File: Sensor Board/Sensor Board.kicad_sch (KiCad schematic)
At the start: 30 parts, among them J1 Programming Header, J4 Micro_SD_Card, U1 PIC18F26K83, U3 SPX3819M5-L-3-3, U4 MCP2562, Y1 12MHz Crystal

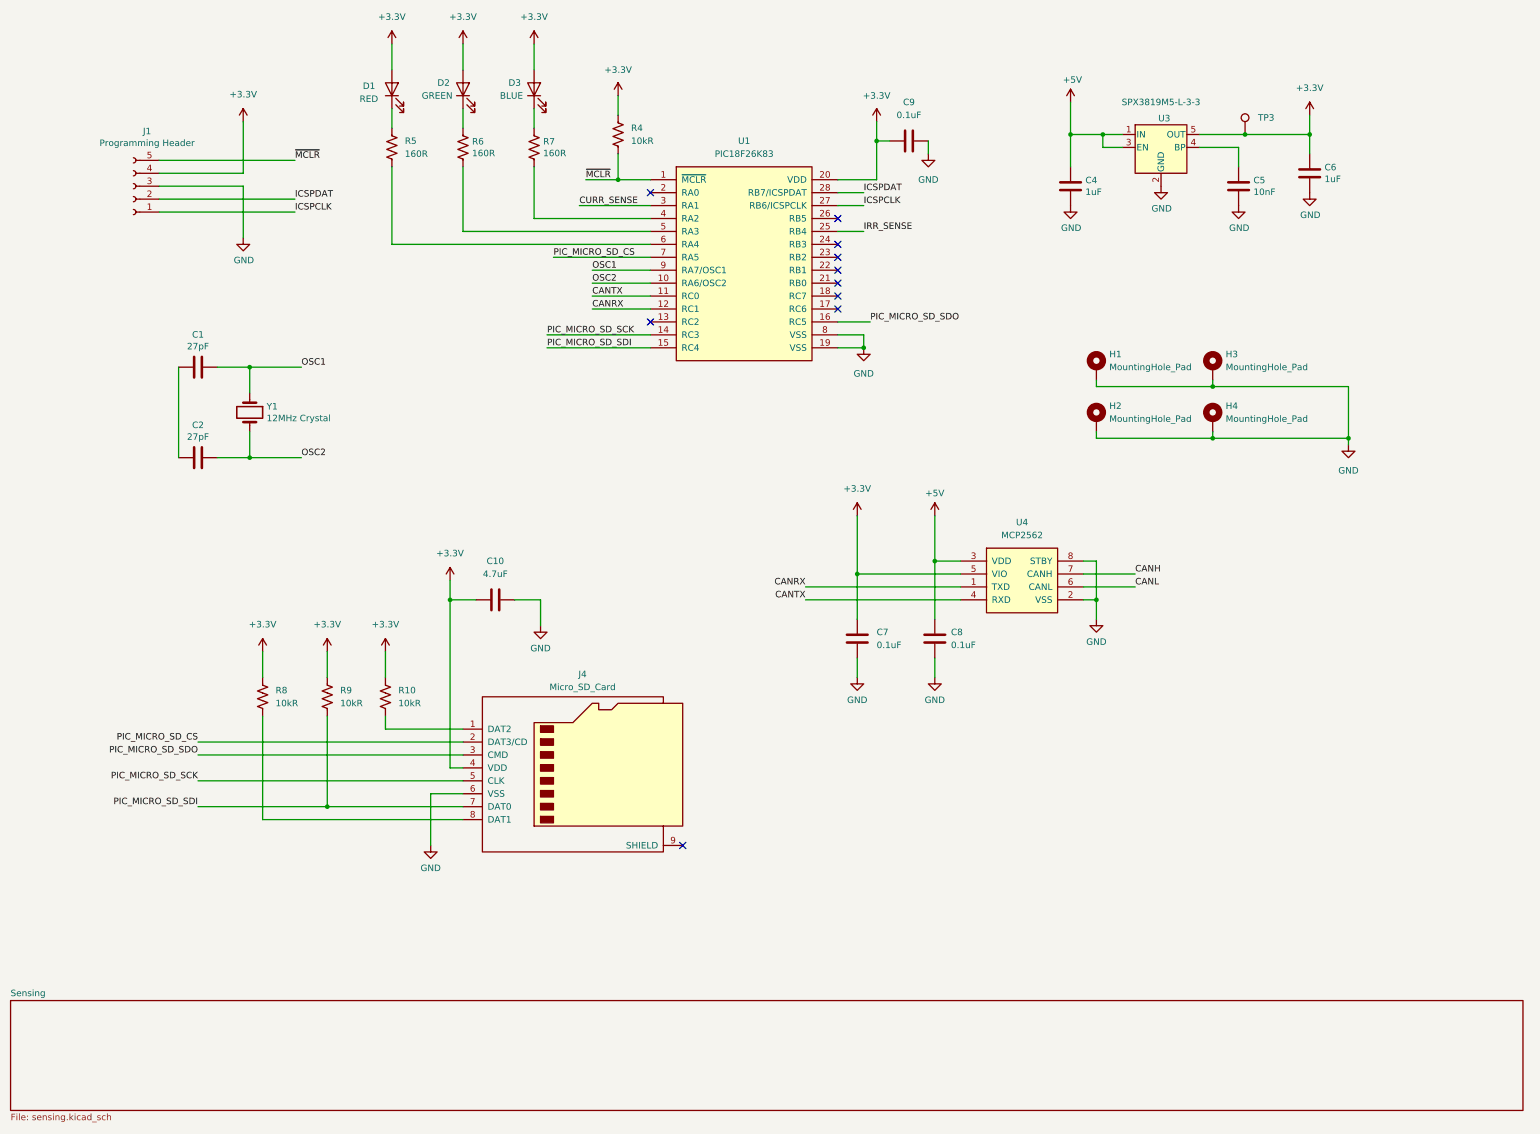
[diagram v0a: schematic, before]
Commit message: Finish schematics and footprint assignments
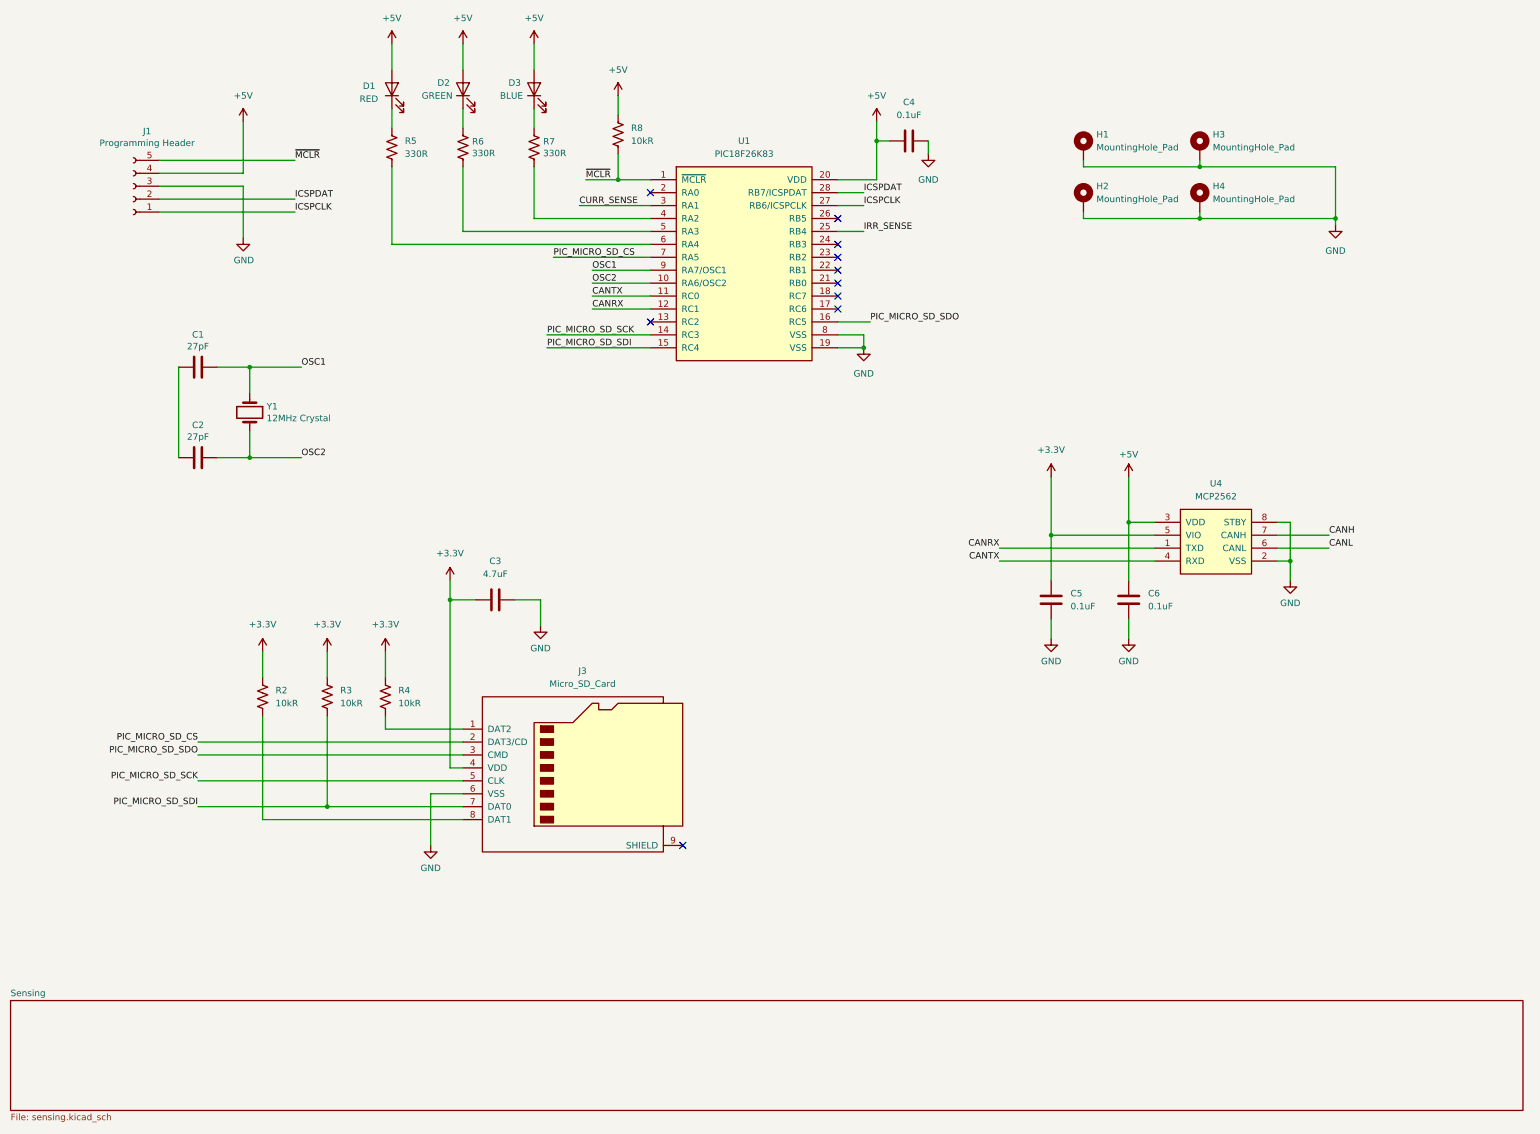
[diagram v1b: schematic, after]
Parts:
- removed C4, C6: 1uF, Capacitor_SMD:C_0805_2012Metric_Pad1.18x1.45mm_HandSolder, symbol Device:C
- removed C5: 10nF, Capacitor_SMD:C_0805_2012Metric_Pad1.18x1.45mm_HandSolder, symbol Device:C
- removed TP3: ~, TestPoint:TestPoint_Pad_1.0x1.0mm, symbol canhw:TestPointDefault
- removed U3: SPX3819M5-L-3-3, Package_TO_SOT_SMD:SOT-23-5, symbol Regulator_Linear:SPX3819M5-L-3-3
- C4: renamed from C9; footprint (none) -> Capacitor_SMD:C_0805_2012Metric_Pad1.18x1.45mm_HandSolder
- J1: footprint canhw:PinHeader_5x2.54_SMD_90deg_952-3198-1-ND -> Canhw:PinSocket_5x2.54_SMD_90deg_952-3198-1-ND
- J3: renamed from J4; footprint canhw:microSD_Molex_WM6698CT-ND -> Canhw:microSD_Molex_WM6698CT-ND
- R5, R6, R7: value 160R -> 330R
- R8: renamed from R4; footprint (none) -> Resistor_SMD:R_0805_2012Metric_Pad1.20x1.40mm_HandSolder
- renumbered C10 to C3, C7 to C5, C8 to C6, R8 to R2, R9 to R3, R10 to R4
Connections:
- net +3.3V: no longer C4.1, D1.2 (A), D2.2 (A), D3.2 (A), J1.4 (Pin_4), R8.1, U1.20 (VDD)
- net +5V: now also C4.1, D1.2 (A), D2.2 (A), D3.2 (A), J1.4 (Pin_4), R8.1, U1.20 (VDD)
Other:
- moved on the sheet: C5, C6, H1, H2, H3, H4, U4

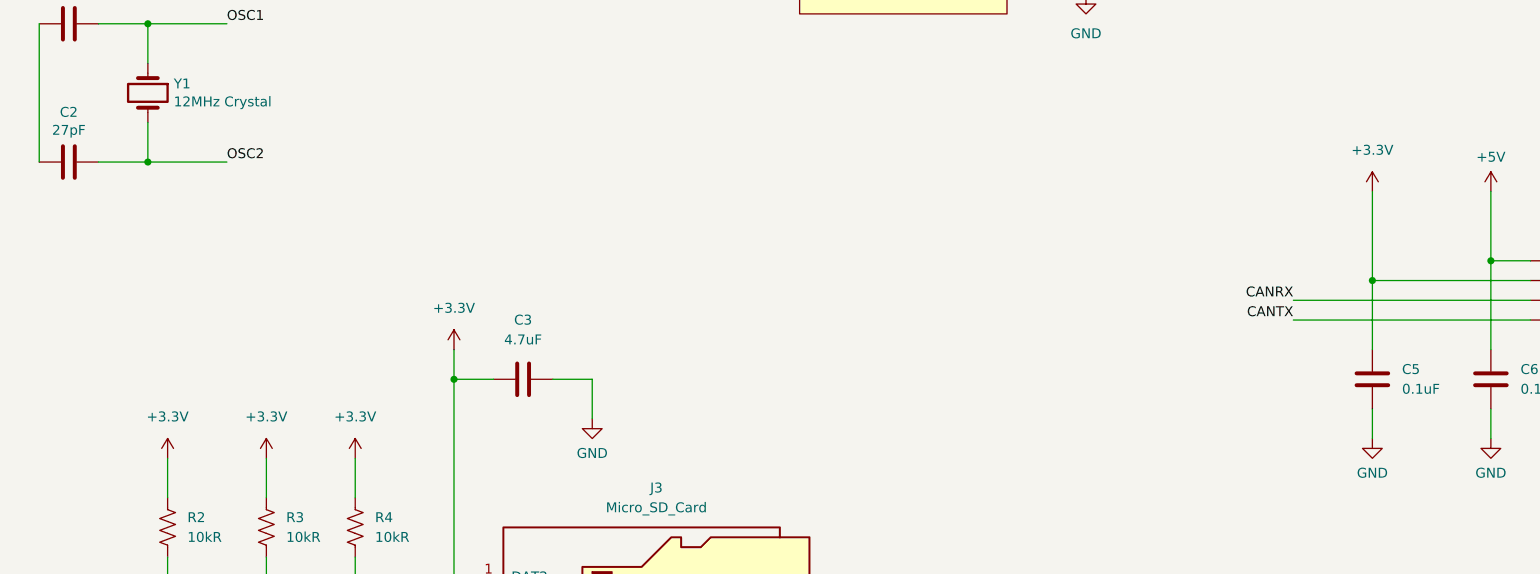
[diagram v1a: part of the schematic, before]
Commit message: Change 3.3v on sensor
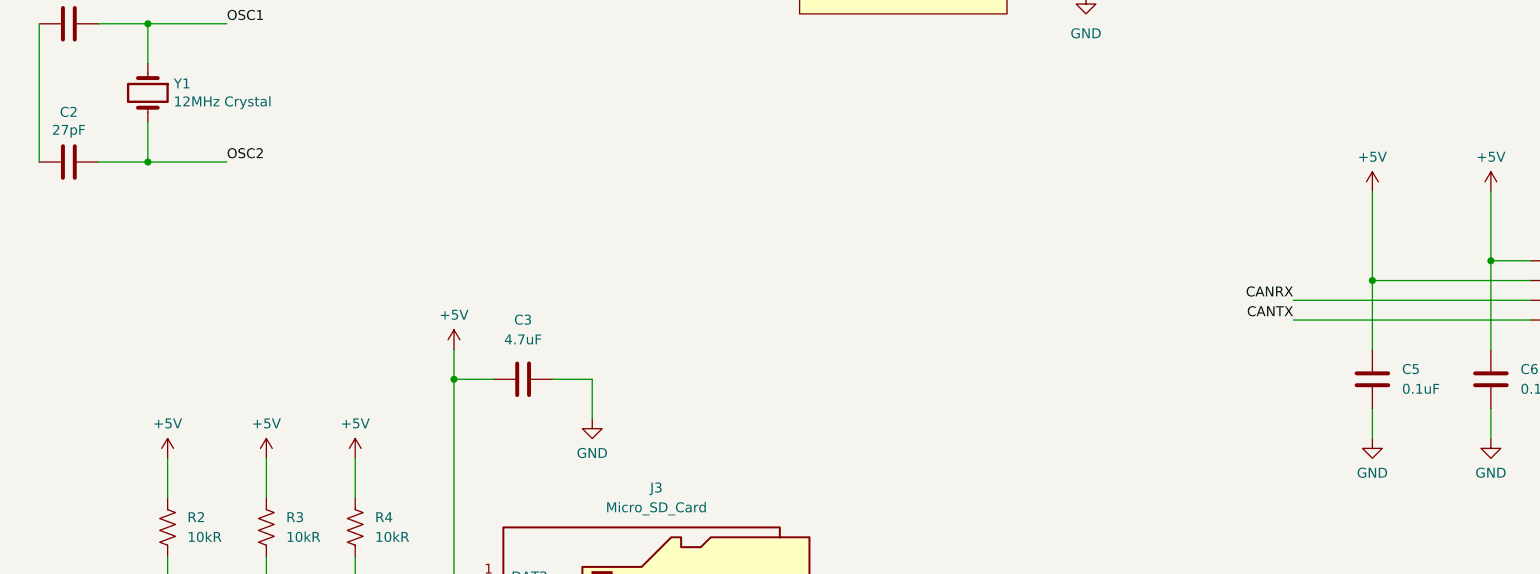
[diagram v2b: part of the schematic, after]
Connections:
- net +3.3V is gone; now on net +5V: C3.2, C5.2, J3.4 (VDD), R2.1, R3.1, R4.1, U4.5 (VIO)

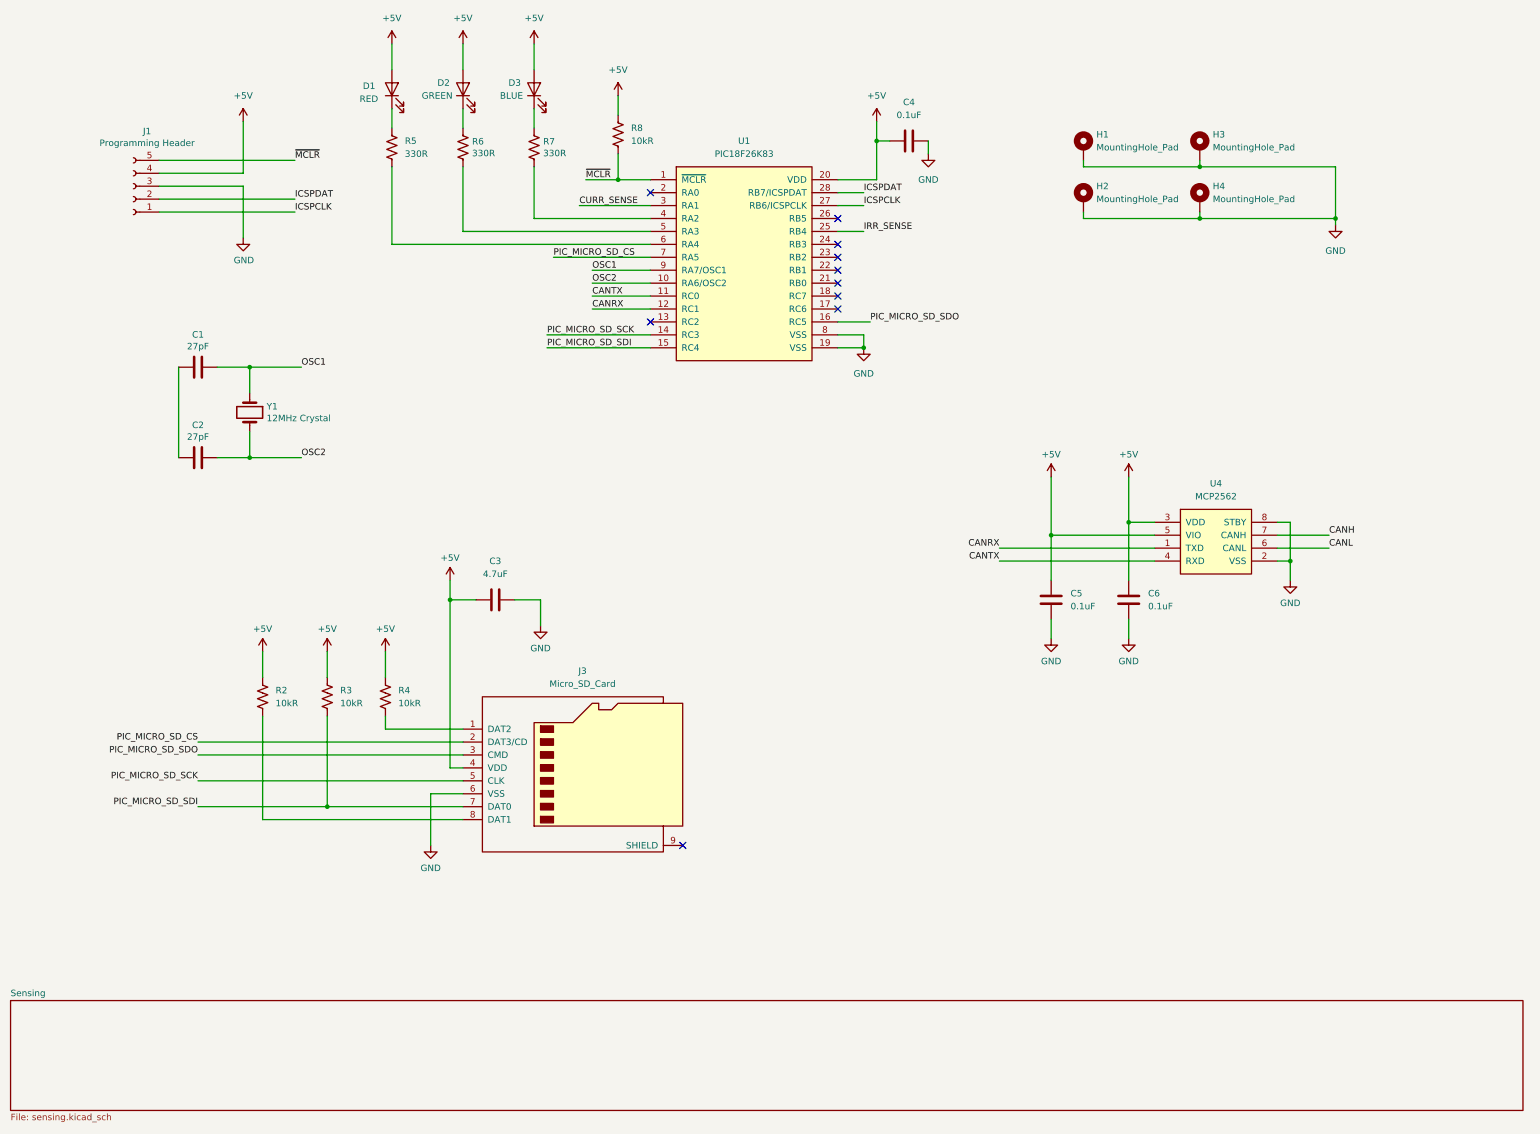
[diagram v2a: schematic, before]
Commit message: fix labels
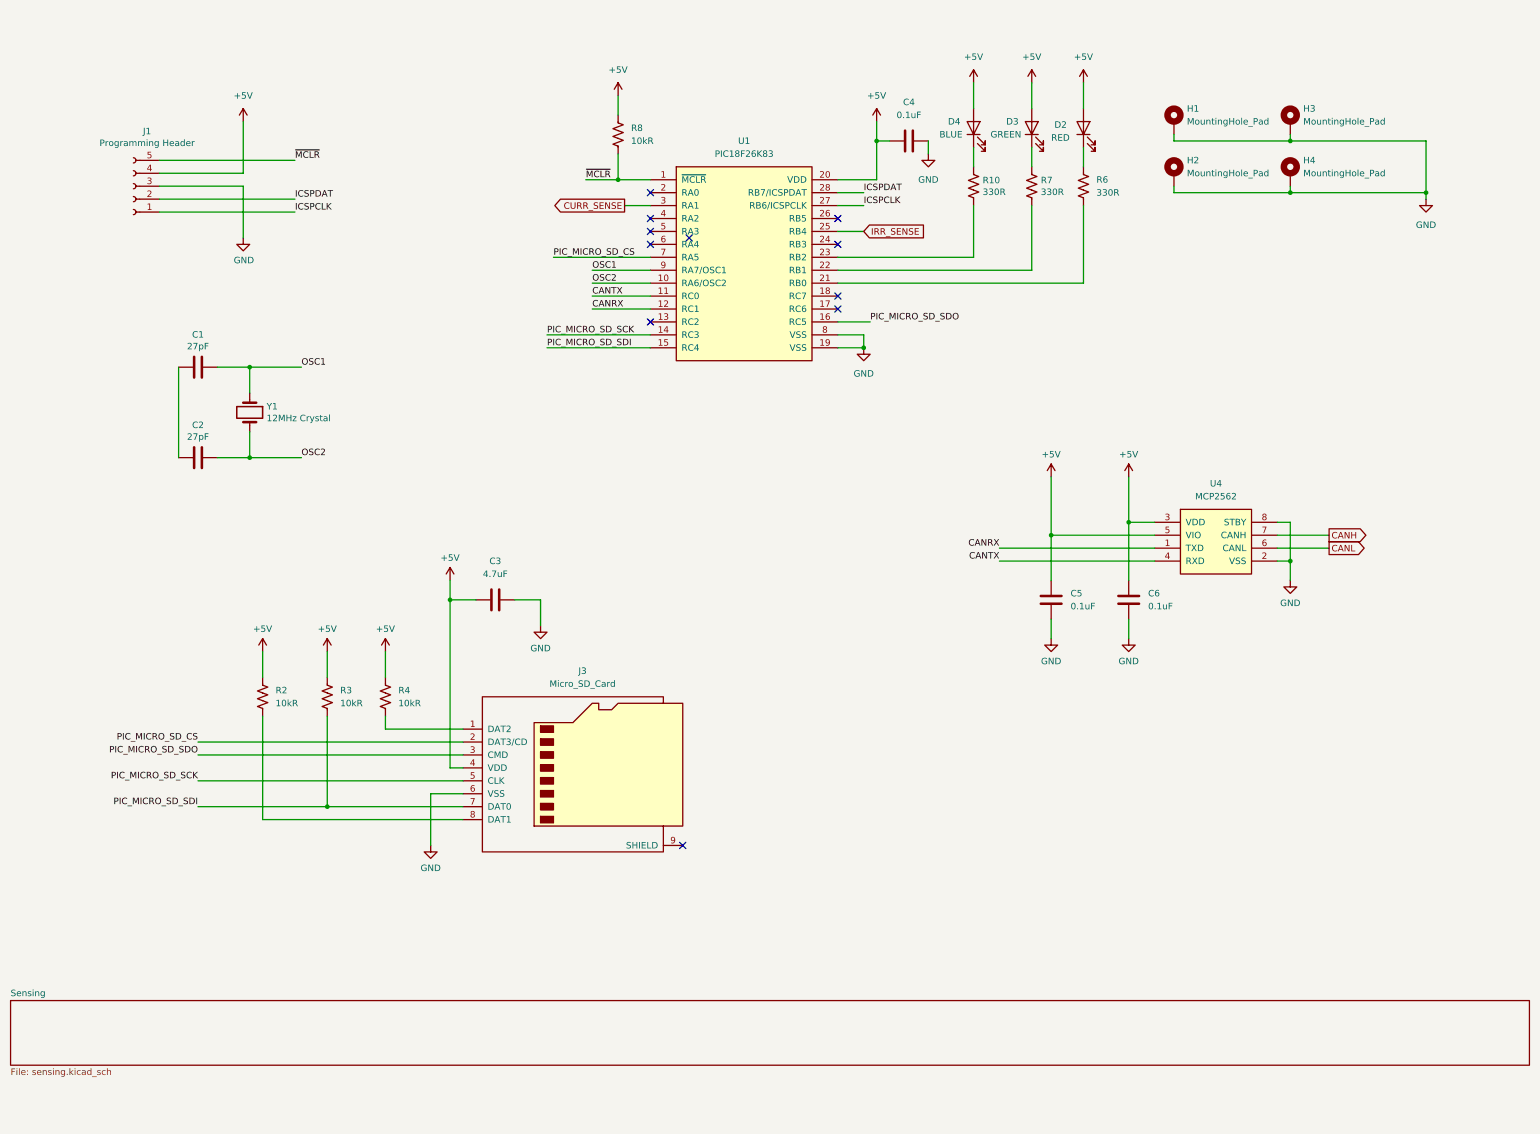
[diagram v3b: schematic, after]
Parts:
- removed D1: RED, LED_SMD:LED_1206_3216Metric_Pad1.42x1.75mm_HandSolder, symbol Device:LED
- removed R5: 330R, Resistor_SMD:R_0805_2012Metric_Pad1.20x1.40mm_HandSolder, symbol Device:R_US
- added D4: BLUE, LED_SMD:LED_1206_3216Metric_Pad1.42x1.75mm_HandSolder, symbol Device:LED
- added R10: 330R, Resistor_SMD:R_0805_2012Metric_Pad1.20x1.40mm_HandSolder, symbol Device:R_US
- D2: value GREEN -> RED; DigiKey 160-1188-1-ND -> 160-1457-1-ND
- D3: value BLUE -> GREEN; DigiKey 1830-1088-1-ND -> 160-1188-1-ND
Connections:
- net +5V: now also D4.2 (A)
- net at U1.21 (RB0): now also R6.2
- net at U1.22 (RB1): now also R7.2
- net at U1.23 (RB2): now also R10.2
- net at U1.4 (RA2): no longer R7.2
- net at U1.5 (RA3): no longer R6.2
- new net: D4.1 (K), R10.1
- no-connect marks 10 -> 11
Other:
- moved on the sheet: H1, H2, H3, H4

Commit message: Fix comments from review
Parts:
- added C10: 10nF, Capacitor_SMD:C_0805_2012Metric_Pad1.18x1.45mm_HandSolder, symbol Device:C
- added C11, C9: 1uF, Capacitor_SMD:C_0805_2012Metric_Pad1.18x1.45mm_HandSolder, symbol Device:C
- added TP1: 5v, TestPoint:TestPoint_Pad_1.5x1.5mm, symbol Connector:TestPoint
- added TP2: 3.3v, TestPoint:TestPoint_Pad_1.5x1.5mm, symbol Connector:TestPoint
- added TP3: TestPoint, TestPoint:TestPoint_Pad_1.5x1.5mm, symbol Connector:TestPoint
- added U3: SPX3819M5-L-3-3, Package_TO_SOT_SMD:SOT-23-5, symbol Regulator_Linear:SPX3819M5-L-3-3
- J3: footprint Canhw:microSD_Molex_WM6698CT-ND -> canhw:microSD_Molex_WM6698CT-ND
- R10, R6, R7: value 330R -> 150R
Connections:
- net +5V: now also C9.1, TP1.1, U3.1 (IN), U3.3 (EN); no longer C3.2, J3.4 (VDD), R2.1, R3.1, R4.1
- net GND: now also C10.2, C11.2, C9.2, U3.2 (GND)
- net IRR_SENSE: now also TP3.1
- new net: C10.1, U3.4 (BP)
- new net +3.3V: C11.1, C3.2, J3.4 (VDD), R2.1, R3.1, R4.1, TP2.1, U3.5 (OUT)
- no-connect marks 11 -> 10

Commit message: Fix review items
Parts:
- J3: footprint canhw:microSD_Molex_WM6698CT-ND -> Canhw:microSD_Molex_WM6698CT-ND
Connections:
- net CANRX: now also U4.4 (RXD); no longer U4.1 (TXD)
- net CANTX: now also U4.1 (TXD); no longer U4.4 (RXD)
- net GND: now also C1.2, C2.2, J3.9 (SHIELD)
- no-connect marks 10 -> 9
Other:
- sheet Sensing ports: added CANH, CANL, CURR_SENSE, IRR_SENSE; removed none
- moved on the sheet: C1, C2, J1, Y1
